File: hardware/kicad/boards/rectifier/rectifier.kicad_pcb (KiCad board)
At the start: 2 copper layers, 146 x 74 mm, 12 parts, among them J1 3-fase ind, J2 V1 ud

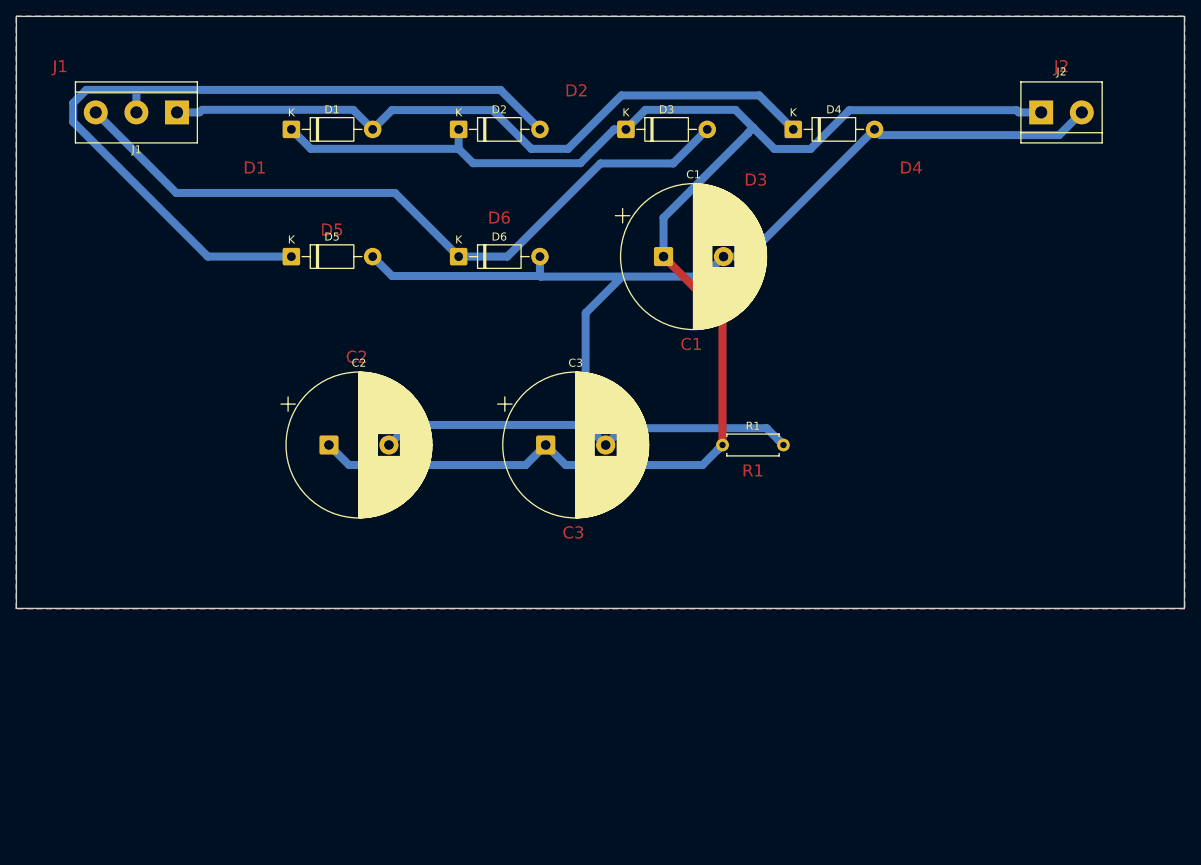
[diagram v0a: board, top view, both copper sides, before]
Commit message: Move all boards to the 104x104 jig format with compact placement
The laser positioning jig takes an exactly 109x109 mm copper blank, so every
board now has identical 104x104 edge cuts (2.5 mm rim). pcb_build.py:
- fixed JIG_W/JIG_H outline, hard failure if content overflows the square
- compact packing: 5 mm bbox gaps (was 8), squarish component cluster below
  the connector zone instead of full-width rows
- mppt/current_sense PLACE layouts re-arranged for the square and tightened

All 7 boards rerouted: 0 unconnected, 0 real DRC errors, and no vias needed
anywhere (the square format routes better than the old elongated boards).
Production DXF/gerbers re-exported; README run-plan updated for the jig
(cut blanks to exactly 109x109, all boards share the same size now).
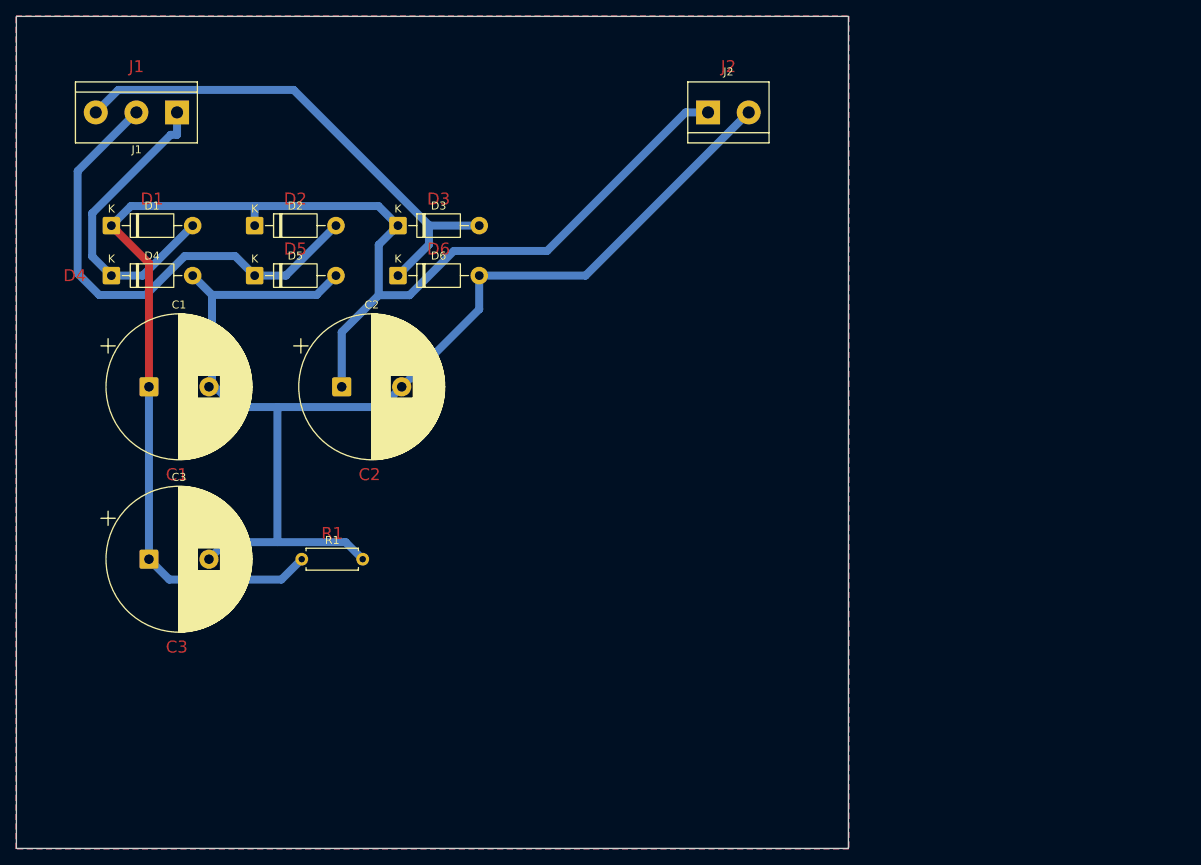
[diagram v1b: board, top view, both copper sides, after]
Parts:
- moved D4 87.2 mm to (31.9, 52.4)
- moved C1 66.3 mm to (36.6, 66.3)
- moved R1 54.5 mm to (55.7, 87.8)
- moved C3 51.6 mm to (36.6, 87.8)
- moved J2 41.6 mm to (106.5, 32.0)
- moved D3 30.9 mm to (67.7, 46.1)
- moved D2 28.2 mm to (49.8, 46.1)
- moved D1 25.5 mm to (31.9, 46.1)
- moved D6 7.95 mm to (67.7, 52.4)
- moved C2 7.45 mm to (60.7, 66.3)
- moved D5 5.17 mm to (49.8, 52.4)
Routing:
- net /PH_A: track 85.7 -> 39.0 mm
- net /PH_B: track 100.5 -> 62.2 mm
- net V1: track 206.4 -> 178.8 mm
- net /PH_C: track 90.5 -> 64.0 mm
- net GND: track 175.7 -> 155.4 mm
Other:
- board size 146 x 74 mm -> 104 x 104 mm

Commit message: Condense and center all boards in the jig outline; reroute drive_circuit
Placement (pcb_build.py): connector columns now hug the component block
instead of sitting at the board edges, and the whole cluster is translated to
the center of the 104x104 outline - nothing sits next to the edge cuts
anymore. Fail-hard check if a cluster outgrows the jig.

drive_circuit keeps the hand-made GUI placement but is rerouted with the
two-stage flow: 43 top tracks + 1 via from the GUI autoroute down to 20
pin-to-pin bridges, no via. New tools/strip_routing.py removes existing
routing textually (sexpdata) - in-process pcbnew Remove() access-violates.

All 7 boards: 0 unconnected, 0 real DRC errors, no vias anywhere; buck is
now fully single-sided (0 top tracks). Production files re-exported.
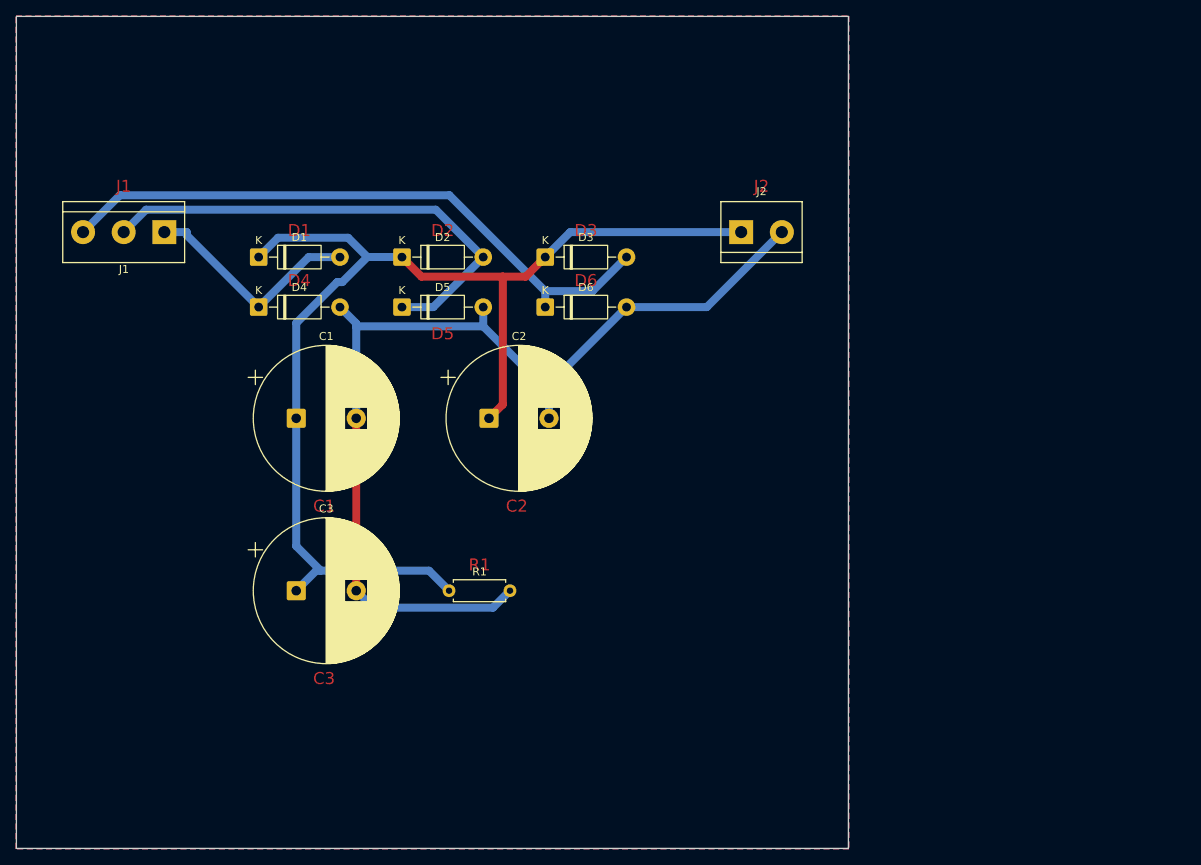
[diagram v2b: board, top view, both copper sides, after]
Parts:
- moved D3 18.8 mm to (86.1, 50.1)
- moved D6 18.8 mm to (86.1, 56.3)
- moved R1 18.8 mm to (74.1, 91.8)
- moved C1 18.8 mm to (55.0, 70.2)
- moved C2 18.8 mm to (79.1, 70.2)
- moved C3 18.8 mm to (55.0, 91.8)
- moved D1 18.8 mm to (50.3, 50.1)
- moved D2 18.8 mm to (68.2, 50.1)
- moved D4 18.8 mm to (50.3, 56.3)
- moved D5 18.8 mm to (68.2, 56.3)
- moved J2 15.5 mm to (110.6, 47.0)
- moved J1 15.0 mm to (38.5, 47.0)
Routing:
- net V1: track 178.8 -> 149.8 mm
- net GND: track 155.4 -> 128.1 mm
- net /PH_C: track 64.0 -> 78.6 mm
- net /PH_A: track 39.0 -> 28.7 mm
- net /PH_B: track 62.2 -> 61.3 mm
